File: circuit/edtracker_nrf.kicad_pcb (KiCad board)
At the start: 2 copper layers, 50 x 44 mm, 17 parts, among them M1 NRF24LE1_SMALL, Q1 TPS1101D, SW1 SW_PUSH, SW2 SWITCH_INV, U1 NRF24LE1_PROG, U2 MPU-6050, U3 UART

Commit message: 
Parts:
- moved C1 4.79 mm to (86.1, 84.6)
- moved C2 4.73 mm to (86.1, 81.2)
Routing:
- net GND: track 31.1 -> 128.3 mm
- net Net-(Q1-Pad1): track 2.50 -> 61.2 mm
- net VCC: track 27.0 -> 77.2 mm
- net /RESET: track 30.4 -> 28.5 mm
- net /FMISO: track 19.0 -> 20.4 mm
- net Net-(M1-Pad8): track 42.6 -> 41.6 mm
- net /PROG: track 35.6 -> 36.2 mm
- net /FSCK: track 15.7 -> 16.3 mm

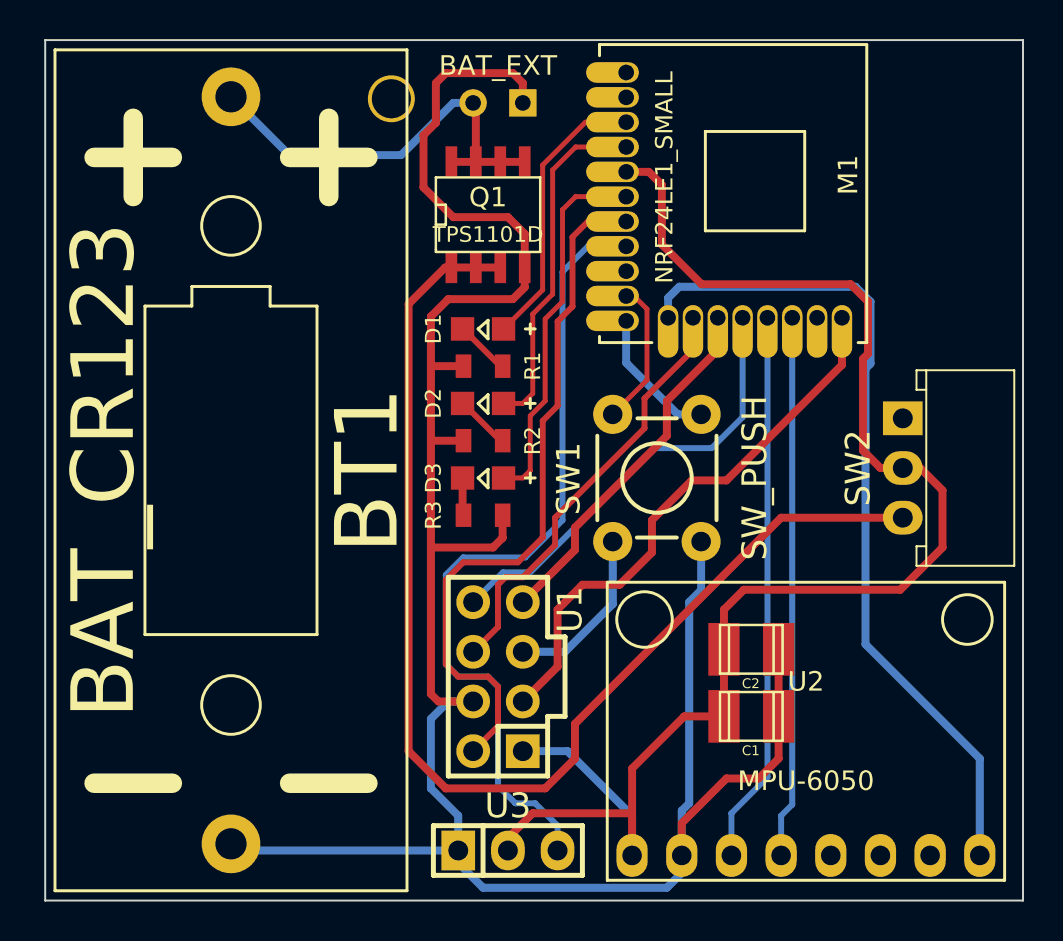
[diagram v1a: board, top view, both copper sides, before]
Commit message: 
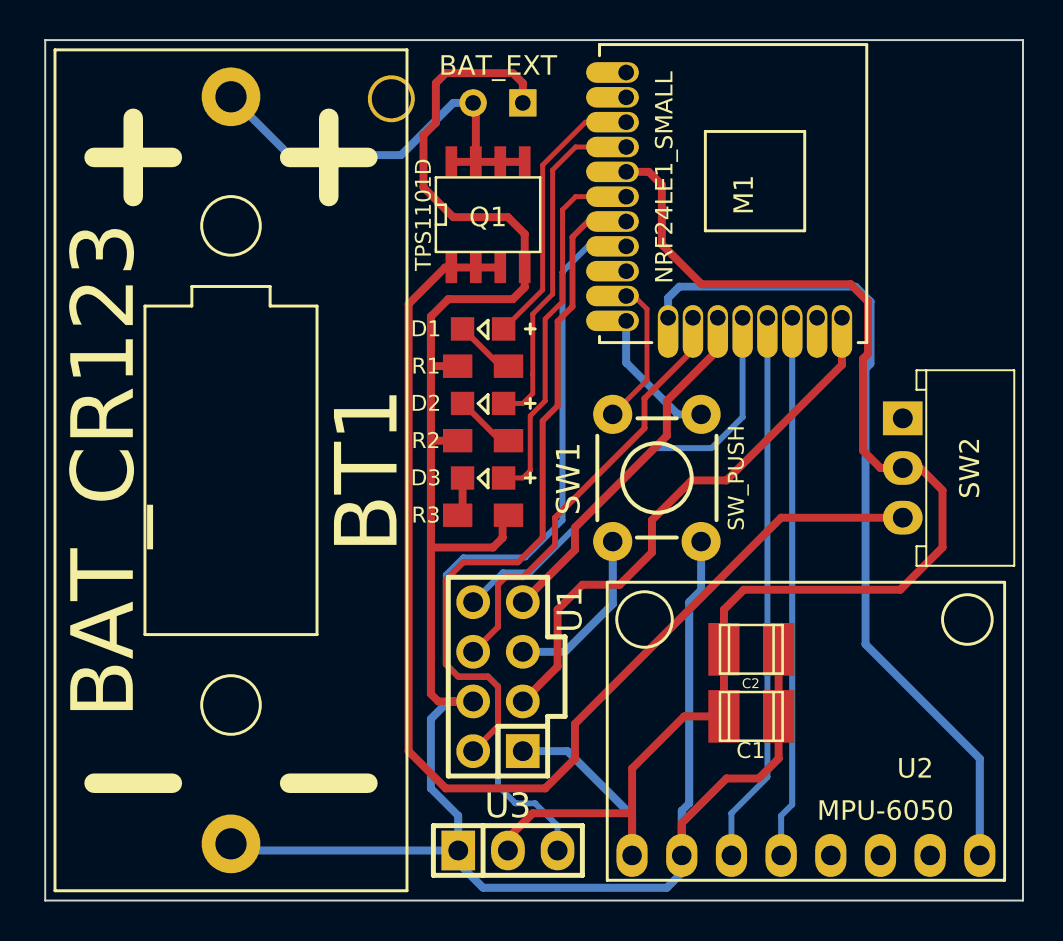
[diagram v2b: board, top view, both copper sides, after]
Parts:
- R1, R2, R3: footprint edtracker_nrf:Resistor_SMD0805_ReflowWave -> edtracker_nrf:Resistor_SMD0805_HandSoldering
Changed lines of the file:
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@@
     (pcb_text_width 0.3)
     (pcb_text_size 1.5 1.5)
-    (mod_edge_width 0.254)
+    (mod_edge_width 0.1778)
     (mod_text_size 1 1)
     (mod_text_width 0.15)
@@
     (descr "1 pin")
     (tags "CONN DEV")
-    (fp_text reference SW2 (at 0 2.286 270) (layer F.SilkS)
-      (effects (font (size 1.27 1.27) (thickness 0.2032)))
+    (fp_text reference SW2 (at 0 -3.429 450) (layer F.SilkS)
+      (effects (font (size 1.016 1.016) (thickness 0.2032)))
     )
     (fp_text value SWITCH_INV (at 0 -2.4 270) (layer F.SilkS) hide
@@
   (module edtracker_nrf:NRF24LE1_SMALL (layer F.Cu)
     (at 85.344 58.166 270)
-    (fp_text reference M1 (at -1.27 -5.715 270) (layer F.SilkS)
+    (fp_text reference M1 (at -0.254 -0.381 270) (layer F.SilkS)
       (effects (font (size 1 1) (thickness 0.15)))
     )
@@
     (descr "SMT capacitor, 1210")
     (fp_text reference C1 (at 0.0254 -1.7526 180) (layer F.SilkS)
-      (effects (font (size 0.50038 0.50038) (thickness 0.11938)))
+      (effects (font (size 0.8128 0.8128) (thickness 0.1524)))
     )
     (fp_text value C (at -0.0254 1.7272 180) (layer F.SilkS) hide
@@
       (effects (font (size 1.2065 1.2065) (thickness 0.127)) (justify left bottom))
     )
-    (fp_text value SW_PUSH (at 0 5 90) (layer F.SilkS)
-      (effects (font (thickness 0.15)))
+    (fp_text value SW_PUSH (at 0 4.064 90) (layer F.SilkS)
+      (effects (font (size 0.8128 0.8128) (thickness 0.1524)))
     )
     (fp_line (start 3.048 -1.016) (end 3.048 -2.54) (layer Dwgs.User) (width 0.2032))
@@
   (module edtracker_nrf:MPU6050 (layer F.Cu)
     (at 88.9 85.344 180)
-    (fp_text reference U2 (at 0 2.54 180) (layer F.SilkS)
+    (fp_text reference U2 (at -5.588 -1.905 180) (layer F.SilkS)
       (effects (font (size 1 1) (thickness 0.15)))
     )
-    (fp_text value MPU-6050 (at 0 -2.54 180) (layer F.SilkS)
+    (fp_text value MPU-6050 (at -4.064 -4.064 180) (layer F.SilkS)
       (effects (font (size 1 1) (thickness 0.15)))
     )
@@
     (tags "CMS SOJ")
     (attr smd)
-    (fp_text reference Q1 (at 0 -0.889) (layer F.SilkS)
+    (fp_text reference Q1 (at 0 0.127) (layer F.SilkS)
       (effects (font (size 1 1) (thickness 0.15)))
     )
-    (fp_text value TPS1101D (at 0 1.016) (layer F.SilkS)
-      (effects (font (size 0.8 0.8) (thickness 0.15)))
+    (fp_text value TPS1101D (at -3.302 0 90) (layer F.SilkS)
+      (effects (font (size 0.8128 0.8128) (thickness 0.1524)))
     )
     (fp_line (start -2.667 1.778) (end -2.667 1.905) (layer F.SilkS) (width 0.127))
@@
       (net 1 GND))
   )
-  (module edtracker_nrf:Resistor_SMD0805_ReflowWave (layer F.Cu)
-    (at 72.39 66.675)
-    (descr "Resistor, SMD, 0805, Reflow, Wave,")
-    (tags "Resistor, SMD, 0805, Reflow, Wave,")
-    (attr smd)
-    (fp_text reference R1 (at 2.54 0 90) (layer F.SilkS)
-      (effects (font (size 0.8128 0.8128) (thickness 0.1778)))
-    )
-    (fp_text value R (at 0 0) (layer F.SilkS) hide
-      (effects (font (size 0.8128 0.8128) (thickness 0.2032)))
-    )
-    (pad 1 smd rect (at -1.00076 0) (size 0.8001 1.19888) (layers F.Cu F.Paste F.Mask)
-      (net 1 GND))
-    (pad 2 smd rect (at 1.00076 0) (size 0.8001 1.19888) (layers F.Cu F.Paste F.Mask)
-      (net 4 "Net-(D1-Pad2)"))
-  )
-  (module edtracker_nrf:Resistor_SMD0805_ReflowWave (layer F.Cu)
-    (at 72.39 70.485)
-    (descr "Resistor, SMD, 0805, Reflow, Wave,")
-    (tags "Resistor, SMD, 0805, Reflow, Wave,")
-    (attr smd)
-    (fp_text reference R2 (at 2.54 0 90) (layer F.SilkS)
-      (effects (font (size 0.8128 0.8128) (thickness 0.1778)))
-    )
-    (fp_text value R (at 0 0) (layer F.SilkS) hide
-      (effects (font (size 0.8128 0.8128) (thickness 0.2032)))
-    )
-    (pad 1 smd rect (at -1.00076 0) (size 0.8001 1.19888) (layers F.Cu F.Paste F.Mask)
-      (net 1 GND))
-    (pad 2 smd rect (at 1.00076 0) (size 0.8001 1.19888) (layers F.Cu F.Paste F.Mask)
-      (net 6 "Net-(D2-Pad2)"))
-  )
-  (module edtracker_nrf:Resistor_SMD0805_ReflowWave (layer F.Cu)
-    (at 72.39 74.295 180)
-    (descr "Resistor, SMD, 0805, Reflow, Wave,")
-    (tags "Resistor, SMD, 0805, Reflow, Wave,")
-    (attr smd)
-    (fp_text reference R3 (at 2.54 0 270) (layer F.SilkS)
-      (effects (font (size 0.8128 0.8128) (thickness 0.1778)))
-    )
-    (fp_text value R (at 0 0 180) (layer F.SilkS) hide
-      (effects (font (size 0.8128 0.8128) (thickness 0.2032)))
-    )
-    (pad 1 smd rect (at -1.00076 0 180) (size 0.8001 1.19888) (layers F.Cu F.Paste F.Mask)
-      (net 1 GND))
-    (pad 2 smd rect (at 1.00076 0 180) (size 0.8001 1.19888) (layers F.Cu F.Paste F.Mask)
-      (net 8 "Net-(D3-Pad2)"))
-  )
   (module edtracker_nrf:LED-0805 (layer F.Cu)
     (at 72.39 64.77 180)
@@
     (tags "LED 0805 SMD")
     (attr smd)
-    (fp_text reference D1 (at 2.54 0 270) (layer F.SilkS)
+    (fp_text reference D1 (at 2.921 0 360) (layer F.SilkS)
       (effects (font (size 0.8128 0.8128) (thickness 0.1778)))
     )
@@
     (tags "LED 0805 SMD")
     (attr smd)
-    (fp_text reference D2 (at 2.54 0 270) (layer F.SilkS)
+    (fp_text reference D2 (at 2.921 0 180) (layer F.SilkS)
       (effects (font (size 0.8128 0.8128) (thickness 0.1778)))
     )
@@
     (tags "LED 0805 SMD")
     (attr smd)
-    (fp_text reference D3 (at 2.54 0 270) (layer F.SilkS)
+    (fp_text reference D3 (at 2.921 0 360) (layer F.SilkS)
       (effects (font (size 0.8128 0.8128) (thickness 0.1778)))
     )
@@
       (net 7 "Net-(D3-Pad1)"))
     (pad 2 smd rect (at 1.04902 0 180) (size 1.19888 1.19888) (layers F.Cu F.Paste F.Mask)
+      (net 8 "Net-(D3-Pad2)"))
+  )
+  (module edtracker_nrf:Resistor_SMD0805_HandSoldering (layer F.Cu)
+    (at 72.39 66.675)
+    (descr "Resistor, SMD, 0805, Hand soldering,")
+    (tags "Resistor, SMD, 0805, Hand soldering,")
+    (attr smd)
+    (fp_text reference R1 (at -2.921 0) (layer F.SilkS)
+      (effects (font (size 0.8128 0.8128) (thickness 0.1778)))
+    )
+    (fp_text value R (at 0.20066 2.60096) (layer F.SilkS) hide
+      (effects (font (size 0.8128 0.8128) (thickness 0.1778)))
+    )
+    (pad 1 smd rect (at -1.30048 0) (size 1.50114 1.19888) (layers F.Cu F.Paste F.Mask)
+      (net 1 GND))
+    (pad 2 smd rect (at 1.30048 0) (size 1.50114 1.19888) (layers F.Cu F.Paste F.Mask)
+      (net 4 "Net-(D1-Pad2)"))
+  )
+  (module edtracker_nrf:Resistor_SMD0805_HandSoldering (layer F.Cu)
+    (at 72.39 70.485)
+    (descr "Resistor, SMD, 0805, Hand soldering,")
+    (tags "Resistor, SMD, 0805, Hand soldering,")
+    (attr smd)
+    (fp_text reference R2 (at -2.921 0) (layer F.SilkS)
+      (effects (font (size 0.8128 0.8128) (thickness 0.1778)))
+    )
+    (fp_text value R (at 0.20066 2.60096) (layer F.SilkS) hide
+      (effects (font (size 0.8128 0.8128) (thickness 0.1778)))
+    )
+    (pad 1 smd rect (at -1.30048 0) (size 1.50114 1.19888) (layers F.Cu F.Paste F.Mask)
+      (net 1 GND))
+    (pad 2 smd rect (at 1.30048 0) (size 1.50114 1.19888) (layers F.Cu F.Paste F.Mask)
+      (net 6 "Net-(D2-Pad2)"))
+  )
+  (module edtracker_nrf:Resistor_SMD0805_HandSoldering (layer F.Cu)
+    (at 72.39 74.295 180)
+    (descr "Resistor, SMD, 0805, Hand soldering,")
+    (tags "Resistor, SMD, 0805, Hand soldering,")
+    (attr smd)
+    (fp_text reference R3 (at 2.921 0 180) (layer F.SilkS)
+      (effects (font (size 0.8128 0.8128) (thickness 0.1778)))
+    )
+    (fp_text value R (at 0.20066 2.60096 180) (layer F.SilkS) hide
+      (effects (font (size 0.8128 0.8128) (thickness 0.1778)))
+    )
+    (pad 1 smd rect (at -1.30048 0 180) (size 1.50114 1.19888) (layers F.Cu F.Paste F.Mask)
+      (net 1 GND))
+    (pad 2 smd rect (at 1.30048 0 180) (size 1.50114 1.19888) (layers F.Cu F.Paste F.Mask)
       (net 8 "Net-(D3-Pad2)"))
   )
@@
   (segment (start 70.452 61.628) (end 68.58 63.5) (width 0.4064) (layer F.Cu) (net 16))
   (segment (start 93.853 74.422) (end 87.63 74.422) (width 0.4064) (layer F.Cu) (net 16))
-  (segment (start 84.3915 64.1985) (end 84.3915 65.8495) (width 0.4064) (layer F.Cu) (net 17) (status C00000))
-  (segment (start 84.3915 65.8495) (end 81.788 68.453) (width 0.4064) (layer F.Cu) (net 17) (status 400000))
-  (segment (start 77.089 76.073) (end 74.422 78.74) (width 0.4064) (layer F.Cu) (net 17) (status 800000))
+  (segment (start 84.3915 64.1985) (end 84.3915 65.8495) (width 0.4064) (layer F.Cu) (net 17))
+  (segment (start 84.3915 65.8495) (end 81.788 68.453) (width 0.4064) (layer F.Cu) (net 17))
+  (segment (start 77.089 76.073) (end 74.422 78.74) (width 0.4064) (layer F.Cu) (net 17))
   (segment (start 77.089 74.93) (end 77.089 76.073) (width 0.4064) (layer F.Cu) (net 17))
   (segment (start 81.788 70.231) (end 77.089 74.93) (width 0.4064) (layer F.Cu) (net 17))

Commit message: 
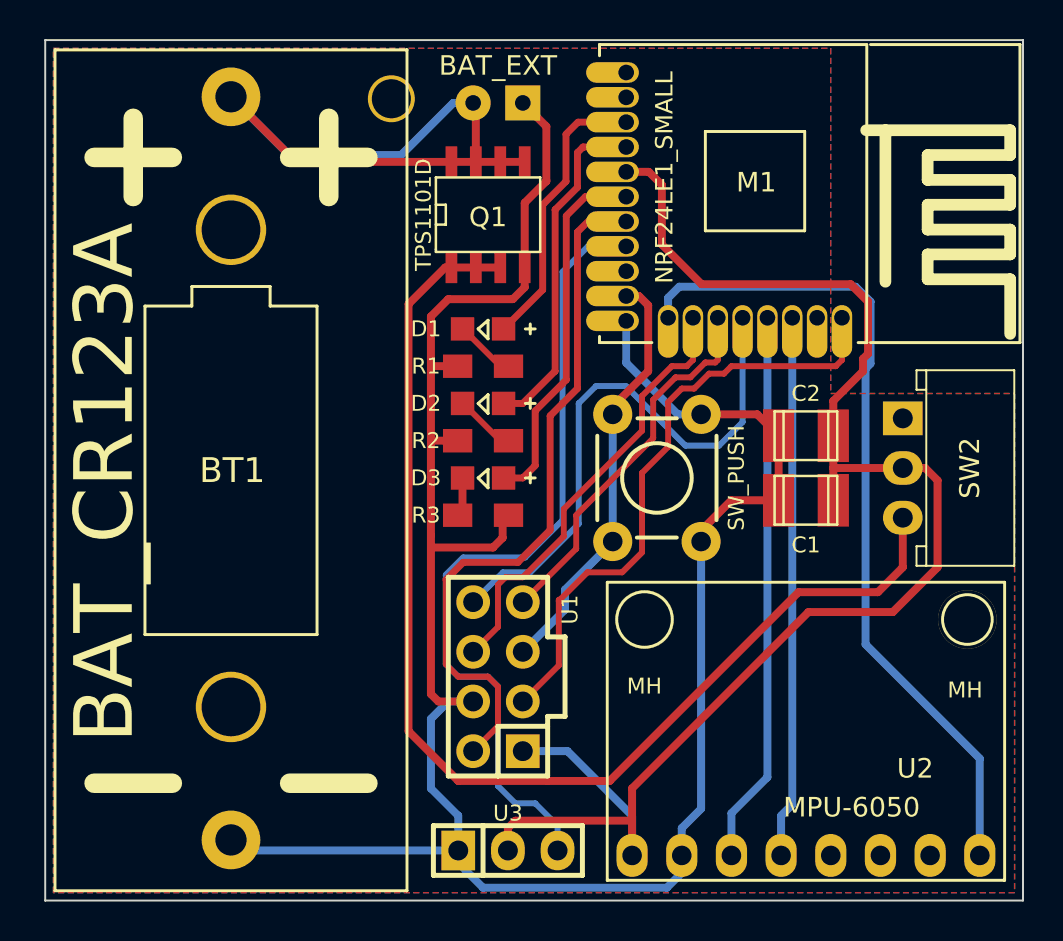
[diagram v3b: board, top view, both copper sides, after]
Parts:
- added G***: OSHW-logo_silkscreen-back_8mm, oshw_logo:OSHW-logo_silkscreen-back_8mm, B.Cu at (57.0, 68.5)
- added MH: MH30, edtracker_nrf:MountingHole_3mm, F.Cu at (80.6, 79.6)
- added MH: MH30, edtracker_nrf:MountingHole_3mm, F.Cu at (97.2, 79.6)
- BT1: value BAT_CR123 -> BAT_CR123A
- moved C1 11.4 mm to (88.9, 73.5), turned to 0 degrees
- moved C2 11.3 mm to (88.9, 70.2), turned to 0 degrees
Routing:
- net Net-(BT1-Pad1): track 21.5 -> 34.2 mm
- net GND: track 128.3 -> 117.6 mm
- net /FCSN: track 24.7 -> 31.0 mm
- net /FSCK: track 16.3 -> 21.7 mm
- net /RESET: track 28.5 -> 31.4 mm
- net VCC: track 77.2 -> 78.2 mm
- net /FMISO: track 20.4 -> 19.4 mm
- added copper zone on B.Cu, net GND
- added copper zone on F.Cu, net GND
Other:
- board text added: "ED Tracker Wireless https://code.google.com/p/edtracker-nrf/ Based on ED Tracker http://edtracker.org.uk/"
